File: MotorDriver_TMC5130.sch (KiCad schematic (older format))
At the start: 17 parts, among them U8 TMC5130

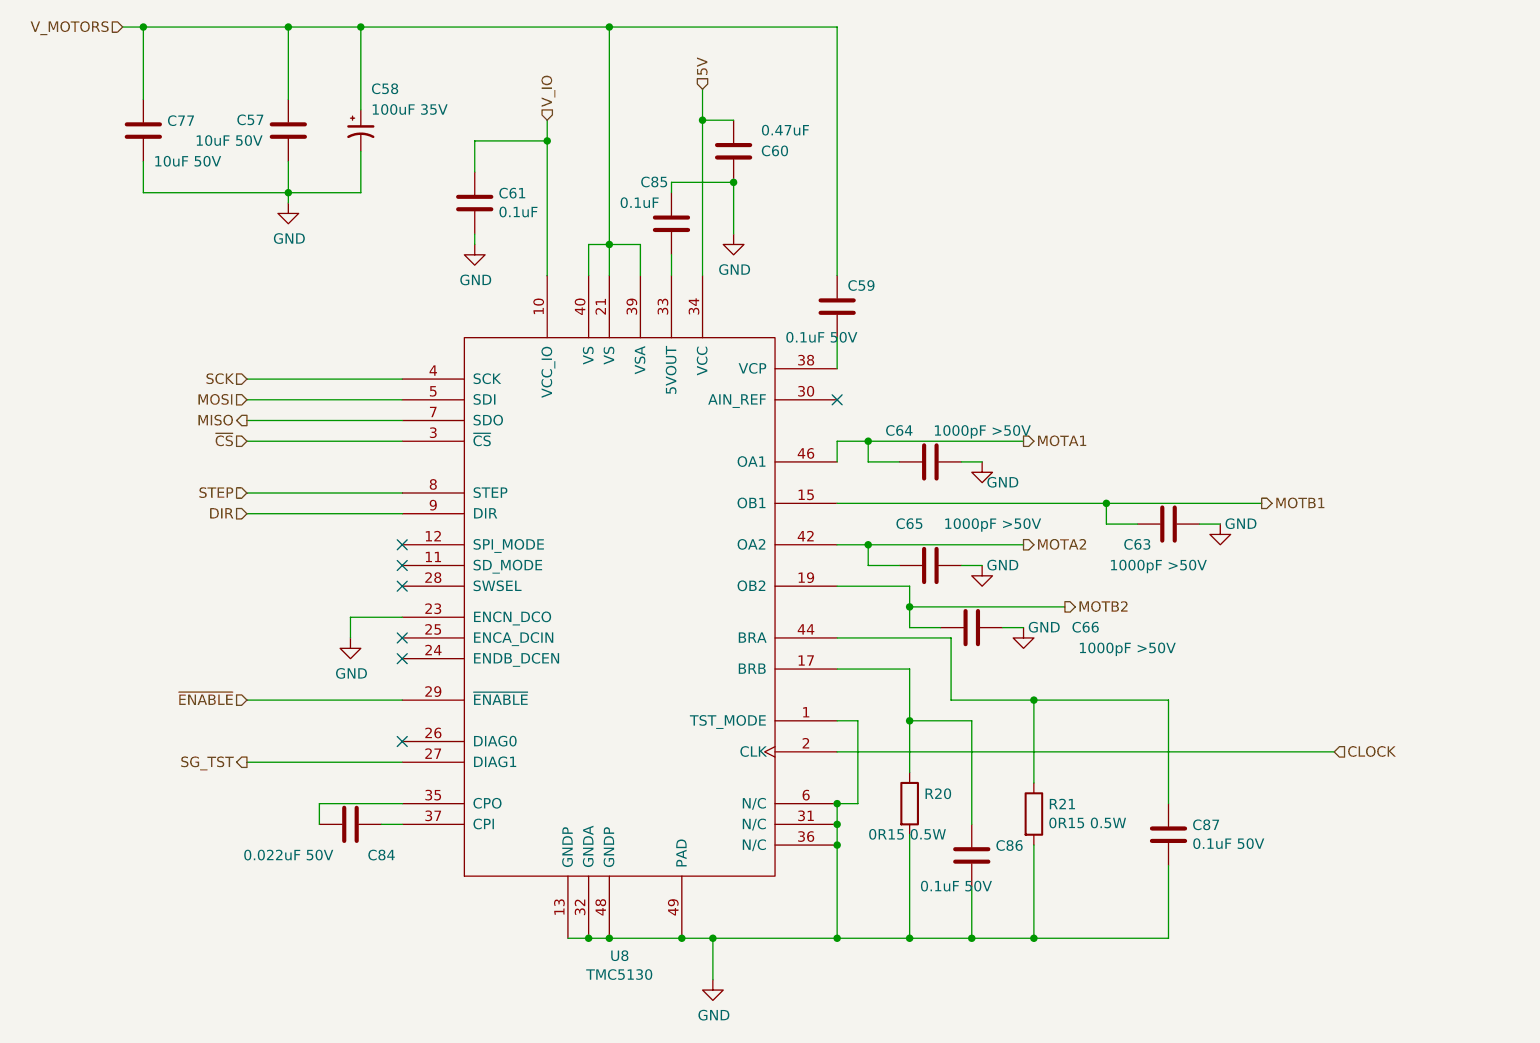
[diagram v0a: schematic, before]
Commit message: Updated schematics with the latest features.
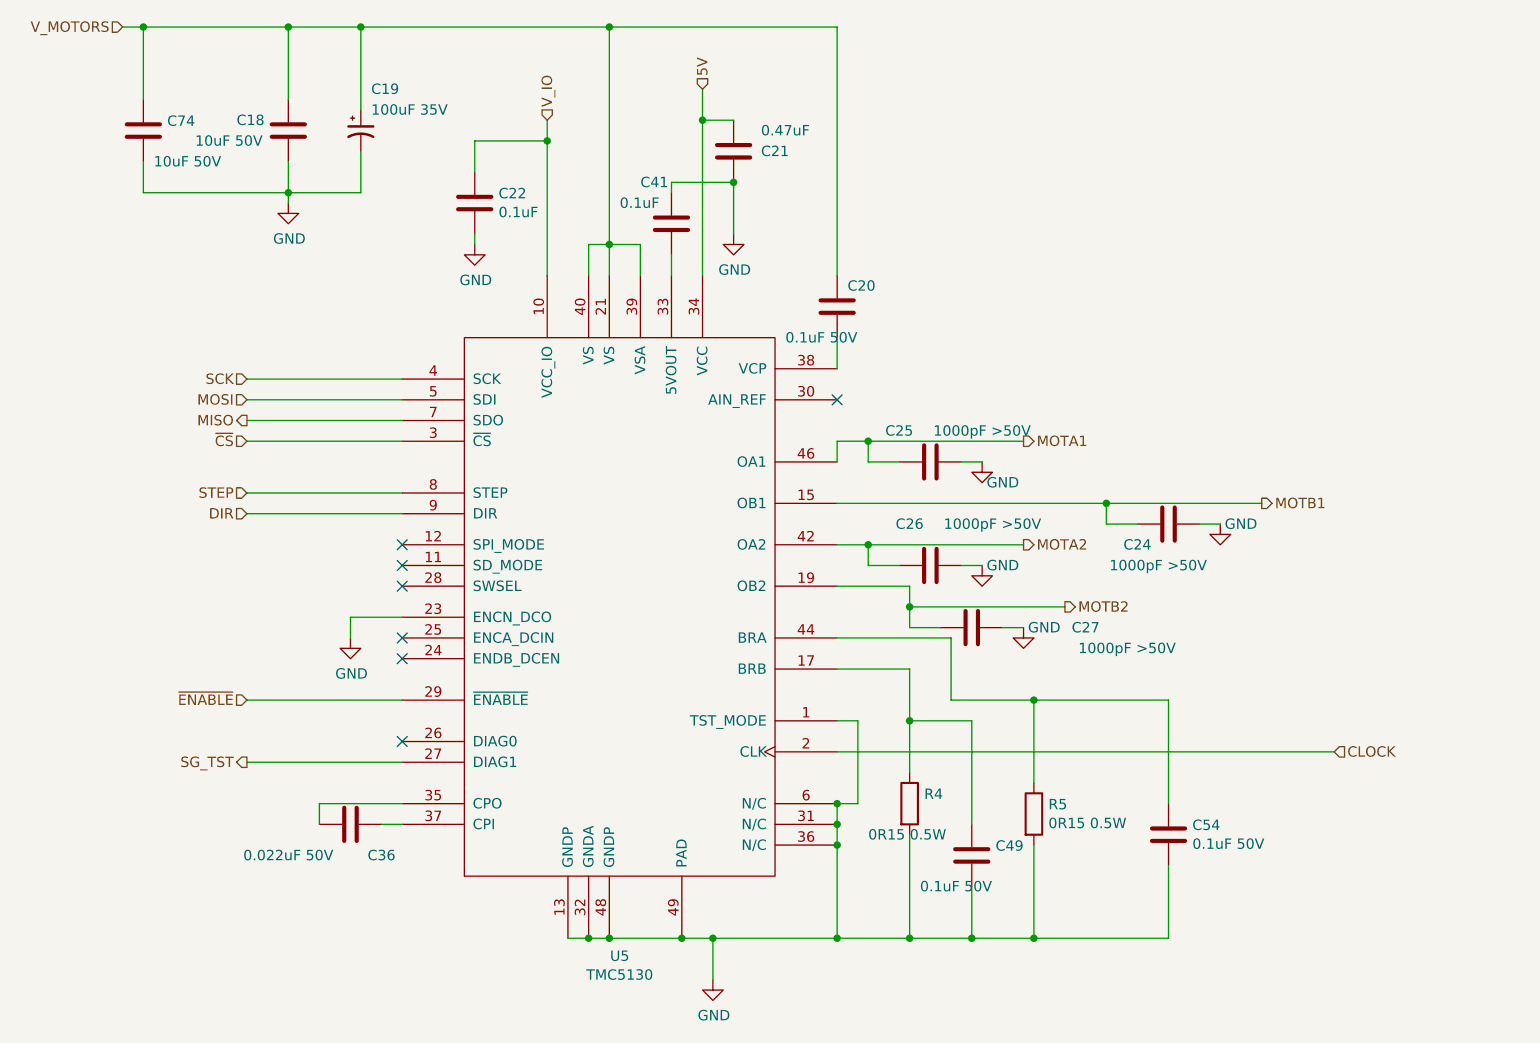
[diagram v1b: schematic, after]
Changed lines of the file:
@@
 $Descr A4 11693 8268
 encoding utf-8
-Sheet 17 35
+Sheet 9 35
 Title ""
 Date ""
@@
 AR Path="/5AC337B6/5ACE1C6D/5ACC0B66/5AC33A94" Ref="C46"  Part="1"
 AR Path="/5AC337B6/5AD9F95A/5AD4B0F5/5AC33A94" Ref="C59"  Part="1"
-F 0 "C59" H 6000 2650 50  0000 L CNN
+F 0 "C20" H 6000 2650 50  0000 L CNN
 F 1 "0.1uF 50V" H 5700 2400 50  0000 L CNN
 F 2 "Capacitor_SMD:C_0402_1005Metric" H 5988 2400 50  0001 C CNN
@@
 AR Path="/5AC337B6/5ACE1C6D/5ACC0B66/5AC33B3C" Ref="C44"  Part="1"
 AR Path="/5AC337B6/5AD9F95A/5AD4B0F5/5AC33B3C" Ref="C57"  Part="1"
-F 0 "C57" H 3050 1750 50  0000 L CNN
+F 0 "C18" H 3050 1750 50  0000 L CNN
 F 1 "10uF 50V" H 2850 1650 50  0000 L CNN
 F 2 "Capacitor_SMD:C_1206_3216Metric" H 3338 1550 50  0001 C CNN
@@
 AR Path="/5AC337B6/5ACE1C6D/5ACC0B66/5AC33B85" Ref="C47"  Part="1"
 AR Path="/5AC337B6/5AD9F95A/5AD4B0F5/5AC33B85" Ref="C60"  Part="1"
-F 0 "C60" H 5250 1800 50  0000 C CNN
+F 0 "C21" H 5250 1800 50  0000 C CNN
 F 1 "0.47uF" H 5200 1700 50  0000 C CNN
 F 2 "Capacitor_SMD:C_0603_1608Metric" H 5488 1650 50  0001 C CNN
@@
 AR Path="/5AC337B6/5ACE1C6D/5ACC0B66/5AC33C56" Ref="C48"  Part="1"
 AR Path="/5AC337B6/5AD9F95A/5AD4B0F5/5AC33C56" Ref="C61"  Part="1"
-F 0 "C61" H 4315 2096 50  0000 L CNN
+F 0 "C22" H 4315 2096 50  0000 L CNN
 F 1 "0.1uF" H 4315 2005 50  0000 L CNN
 F 2 "Capacitor_SMD:C_0603_1608Metric" H 4238 1900 50  0001 C CNN
@@
 AR Path="/5AC337B6/5ACE1C6D/5ACC0B66/5AC33CA1" Ref="C50"  Part="1"
 AR Path="/5AC337B6/5AD9F95A/5AD4B0F5/5AC33CA1" Ref="C63"  Part="1"
-F 0 "C63" V 7650 3450 50  0000 C CNN
+F 0 "C24" V 7650 3450 50  0000 C CNN
 F 1 "1000pF >50V" V 7750 3550 50  0000 C CNN
 F 2 "Capacitor_SMD:C_0603_1608Metric" H 7588 3450 50  0001 C CNN
@@
 AR Path="/5AC337B6/5ACE1C6D/5ACC0B66/5AC33D6E" Ref="C51"  Part="1"
 AR Path="/5AC337B6/5AD9F95A/5AD4B0F5/5AC33D6E" Ref="C64"  Part="1"
-F 0 "C64" V 6250 3150 50  0000 C CNN
+F 0 "C25" V 6250 3150 50  0000 C CNN
 F 1 "1000pF >50V" V 6250 3550 50  0000 C CNN
 F 2 "Capacitor_SMD:C_0603_1608Metric" H 6438 3150 50  0001 C CNN
@@
 AR Path="/5AC337B6/5ACE1C6D/5ACC0B66/5AC33DC1" Ref="C52"  Part="1"
 AR Path="/5AC337B6/5AD9F95A/5AD4B0F5/5AC33DC1" Ref="C65"  Part="1"
-F 0 "C65" V 6200 3700 50  0000 C CNN
+F 0 "C26" V 6200 3700 50  0000 C CNN
 F 1 "1000pF >50V" V 6200 4100 50  0000 C CNN
 F 2 "Capacitor_SMD:C_0603_1608Metric" H 6438 3650 50  0001 C CNN
@@
 AR Path="/5AC337B6/5ACE1C6D/5ACC0B66/5AC33E6E" Ref="C53"  Part="1"
 AR Path="/5AC337B6/5AD9F95A/5AD4B0F5/5AC33E6E" Ref="C66"  Part="1"
-F 0 "C66" V 6600 4650 50  0000 C CNN
+F 0 "C27" V 6600 4650 50  0000 C CNN
 F 1 "1000pF >50V" V 6700 4850 50  0000 C CNN
 F 2 "Capacitor_SMD:C_0603_1608Metric" H 6638 3950 50  0001 C CNN
@@
 AR Path="/5AC337B6/5ACE1C6D/5ACC0B66/5AC34593" Ref="#PWR049"  Part="1"
 AR Path="/5AC337B6/5AD9F95A/5AD4B0F5/5AC34593" Ref="#PWR059"  Part="1"
-F 0 "#PWR059" H 5450 1950 50  0001 C CNN
+F 0 "#PWR027" H 5450 1950 50  0001 C CNN
 F 1 "GND" H 5455 2027 50  0000 C CNN
 F 2 "" H 5450 2200 50  0001 C CNN
@@
 AR Path="/5AC337B6/5ACE1C6D/5ACC0B66/5AC345D6" Ref="#PWR048"  Part="1"
 AR Path="/5AC337B6/5AD9F95A/5AD4B0F5/5AC345D6" Ref="#PWR058"  Part="1"
-F 0 "#PWR058" H 3300 1800 50  0001 C CNN
+F 0 "#PWR026" H 3300 1800 50  0001 C CNN
 F 1 "GND" H 3305 1877 50  0000 C CNN
 F 2 "" H 3300 2050 50  0001 C CNN
@@
 AR Path="/5AC337B6/5ACE1C6D/5ACC0B66/5AC34619" Ref="#PWR050"  Part="1"
 AR Path="/5AC337B6/5AD9F95A/5AD4B0F5/5AC34619" Ref="#PWR060"  Part="1"
-F 0 "#PWR060" H 7800 3350 50  0001 C CNN
+F 0 "#PWR028" H 7800 3350 50  0001 C CNN
 F 1 "GND" H 7900 3600 50  0000 C CNN
 F 2 "" H 7800 3600 50  0001 C CNN
@@
 AR Path="/5AC337B6/5ACE1C6D/5ACC0B66/5AC3465C" Ref="#PWR051"  Part="1"
 AR Path="/5AC337B6/5AD9F95A/5AD4B0F5/5AC3465C" Ref="#PWR061"  Part="1"
-F 0 "#PWR061" H 6650 3050 50  0001 C CNN
+F 0 "#PWR029" H 6650 3050 50  0001 C CNN
 F 1 "GND" H 6750 3200 50  0000 C CNN
 F 2 "" H 6650 3300 50  0001 C CNN
@@
 AR Path="/5AC337B6/5ACE1C6D/5ACC0B66/5AC3469F" Ref="#PWR052"  Part="1"
 AR Path="/5AC337B6/5AD9F95A/5AD4B0F5/5AC3469F" Ref="#PWR062"  Part="1"
-F 0 "#PWR062" H 6650 3550 50  0001 C CNN
+F 0 "#PWR030" H 6650 3550 50  0001 C CNN
 F 1 "GND" H 6750 3800 50  0000 C CNN
 F 2 "" H 6650 3800 50  0001 C CNN
@@
 AR Path="/5AC337B6/5ACE1C6D/5ACC0B66/5AC346E2" Ref="#PWR053"  Part="1"
 AR Path="/5AC337B6/5AD9F95A/5AD4B0F5/5AC346E2" Ref="#PWR063"  Part="1"
-F 0 "#PWR063" H 6850 3850 50  0001 C CNN
+F 0 "#PWR031" H 6850 3850 50  0001 C CNN
 F 1 "GND" H 6950 4100 50  0000 C CNN
 F 2 "" H 6850 4100 50  0001 C CNN
@@
 AR Path="/5AC337B6/5ACE1C6D/5ACC0B66/5AC34725" Ref="#PWR047"  Part="1"
 AR Path="/5AC337B6/5AD9F95A/5AD4B0F5/5AC34725" Ref="#PWR057"  Part="1"
-F 0 "#PWR057" H 5350 5550 50  0001 C CNN
+F 0 "#PWR025" H 5350 5550 50  0001 C CNN
 F 1 "GND" H 5355 5627 50  0000 C CNN
 F 2 "" H 5350 5800 50  0001 C CNN
@@
 AR Path="/5AC337B6/5ACE1C6D/5ACC0B66/5AC55FA7" Ref="C45"  Part="1"
 AR Path="/5AC337B6/5AD9F95A/5AD4B0F5/5AC55FA7" Ref="C58"  Part="1"
-F 0 "C58" H 3700 1900 50  0000 L CNN
+F 0 "C19" H 3700 1900 50  0000 L CNN
 F 1 "100uF 35V" H 3700 1800 50  0000 L CNN
 F 2 "Capacitor_SMD:CP_Elec_6.3x7.7" H 3650 1700 50  0001 C CNN
@@
 AR Path="/5AC337B6/5ACE1C6D/5ACC0B66/5ACA36B2" Ref="C76"  Part="1"
 AR Path="/5AC337B6/5AD9F95A/5AD4B0F5/5ACA36B2" Ref="C77"  Part="1"
-F 0 "C77" H 2715 1746 50  0000 L CNN
+F 0 "C74" H 2715 1746 50  0000 L CNN
 F 1 "10uF 50V" H 2650 1550 50  0000 L CNN
 F 2 "Capacitor_SMD:C_1206_3216Metric" H 2638 1550 50  0001 C CNN
@@
 AR Path="/5AC337B6/5ACCA309/5ACC0B66/5ACFA54E" Ref="U6"  Part="1"
 AR Path="/5AC337B6/5ACE1C6D/5ACC0B66/5ACFA54E" Ref="U7"  Part="1"
-F 0 "U8" H 4900 1714 50  0000 C CNN
+F 0 "U5" H 4900 1714 50  0000 C CNN
 F 1 "TMC5130" H 4900 1623 50  0000 C CNN
 F 2 "PrntrBoardV1:tmc5130-nc" H 4900 3700 50  0001 C CNN
@@
 AR Path="/5AC337B6/5ACCA309/5ACC0B66/5AD3397E" Ref="#PWR081"  Part="1"
 AR Path="/5AC337B6/5ACE1C6D/5ACC0B66/5AD3397E" Ref="#PWR083"  Part="1"
-F 0 "#PWR085" H 4200 2000 50  0001 C CNN
+F 0 "#PWR079" H 4200 2000 50  0001 C CNN
 F 1 "GND" H 4205 2077 50  0000 C CNN
 F 2 "" H 4200 2250 50  0001 C CNN
@@
 AR Path="/5AC337B6/5ACCA309/5ACC0B66/5AD37DE9" Ref="C67"  Part="1"
 AR Path="/5AC337B6/5ACE1C6D/5ACC0B66/5AD37DE9" Ref="C81"  Part="1"
-F 0 "C85" H 5000 2350 50  0000 L CNN
+F 0 "C41" H 5000 2350 50  0000 L CNN
 F 1 "0.1uF" H 4900 2250 50  0000 L CNN
 F 2 "Capacitor_SMD:C_0603_1608Metric" H 5188 2000 50  0001 C CNN
@@
 AR Path="/5AC337B6/5ACCA309/5ACC0B66/5AD494C8" Ref="C62"  Part="1"
 AR Path="/5AC337B6/5ACE1C6D/5ACC0B66/5AD494C8" Ref="C80"  Part="1"
-F 0 "C84" V 3750 5200 50  0000 C CNN
+F 0 "C36" V 3750 5200 50  0000 C CNN
 F 1 "0.022uF 50V" V 3750 4750 50  0000 C CNN
 F 2 "Capacitor_SMD:C_0603_1608Metric" H 3638 4900 50  0001 C CNN
@@
 AR Path="/5AC337B6/5ACCA309/5ACC0B66/5AD5670C" Ref="#PWR080"  Part="1"
 AR Path="/5AC337B6/5ACE1C6D/5ACC0B66/5AD5670C" Ref="#PWR082"  Part="1"
-F 0 "#PWR084" H 3600 3900 50  0001 C CNN
+F 0 "#PWR078" H 3600 3900 50  0001 C CNN
 F 1 "GND" H 3605 3977 50  0000 C CNN
 F 2 "" H 3600 4150 50  0001 C CNN
@@
 AR Path="/5AC337B6/5ACCA309/5ACC0B66/5AD66FAA" Ref="R12"  Part="1"
 AR Path="/5AC337B6/5ACE1C6D/5ACC0B66/5AD66FAA" Ref="R14"  Part="1"
-F 0 "R20" H 6370 4996 50  0000 L CNN
+F 0 "R4" H 6370 4996 50  0000 L CNN
 F 1 "0R15 0.5W" H 6100 4800 50  0000 L CNN
 F 2 "Resistor_SMD:R_1206_3216Metric" V 6230 4950 50  0001 C CNN
@@
 AR Path="/5AC337B6/5ACCA309/5ACC0B66/5AD67008" Ref="R13"  Part="1"
 AR Path="/5AC337B6/5ACE1C6D/5ACC0B66/5AD67008" Ref="R15"  Part="1"
-F 0 "R21" H 6970 5046 50  0000 L CNN
+F 0 "R5" H 6970 5046 50  0000 L CNN
 F 1 "0R15 0.5W" H 6970 4955 50  0000 L CNN
 F 2 "Resistor_SMD:R_1206_3216Metric" V 6830 5000 50  0001 C CNN
@@
 AR Path="/5AC337B6/5ACCA309/5ACC0B66/5AD6F856" Ref="C79"  Part="1"
 AR Path="/5AC337B6/5ACE1C6D/5ACC0B66/5AD6F856" Ref="C83"  Part="1"
-F 0 "C87" H 7665 5146 50  0000 L CNN
+F 0 "C54" H 7665 5146 50  0000 L CNN
 F 1 "0.1uF 50V" H 7665 5055 50  0000 L CNN
 F 2 "Capacitor_SMD:C_0402_1005Metric" H 7588 4950 50  0001 C CNN
@@
 AR Path="/5AC337B6/5ACCA309/5ACC0B66/5AD6F966" Ref="C78"  Part="1"
 AR Path="/5AC337B6/5ACE1C6D/5ACC0B66/5AD6F966" Ref="C82"  Part="1"
-F 0 "C86" H 6715 5246 50  0000 L CNN
+F 0 "C49" H 6715 5246 50  0000 L CNN
 F 1 "0.1uF 50V" H 6350 5050 50  0000 L CNN
 F 2 "Capacitor_SMD:C_0402_1005Metric" H 6638 5050 50  0001 C CNN

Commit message: Add missing files from the TMC2130 branch.
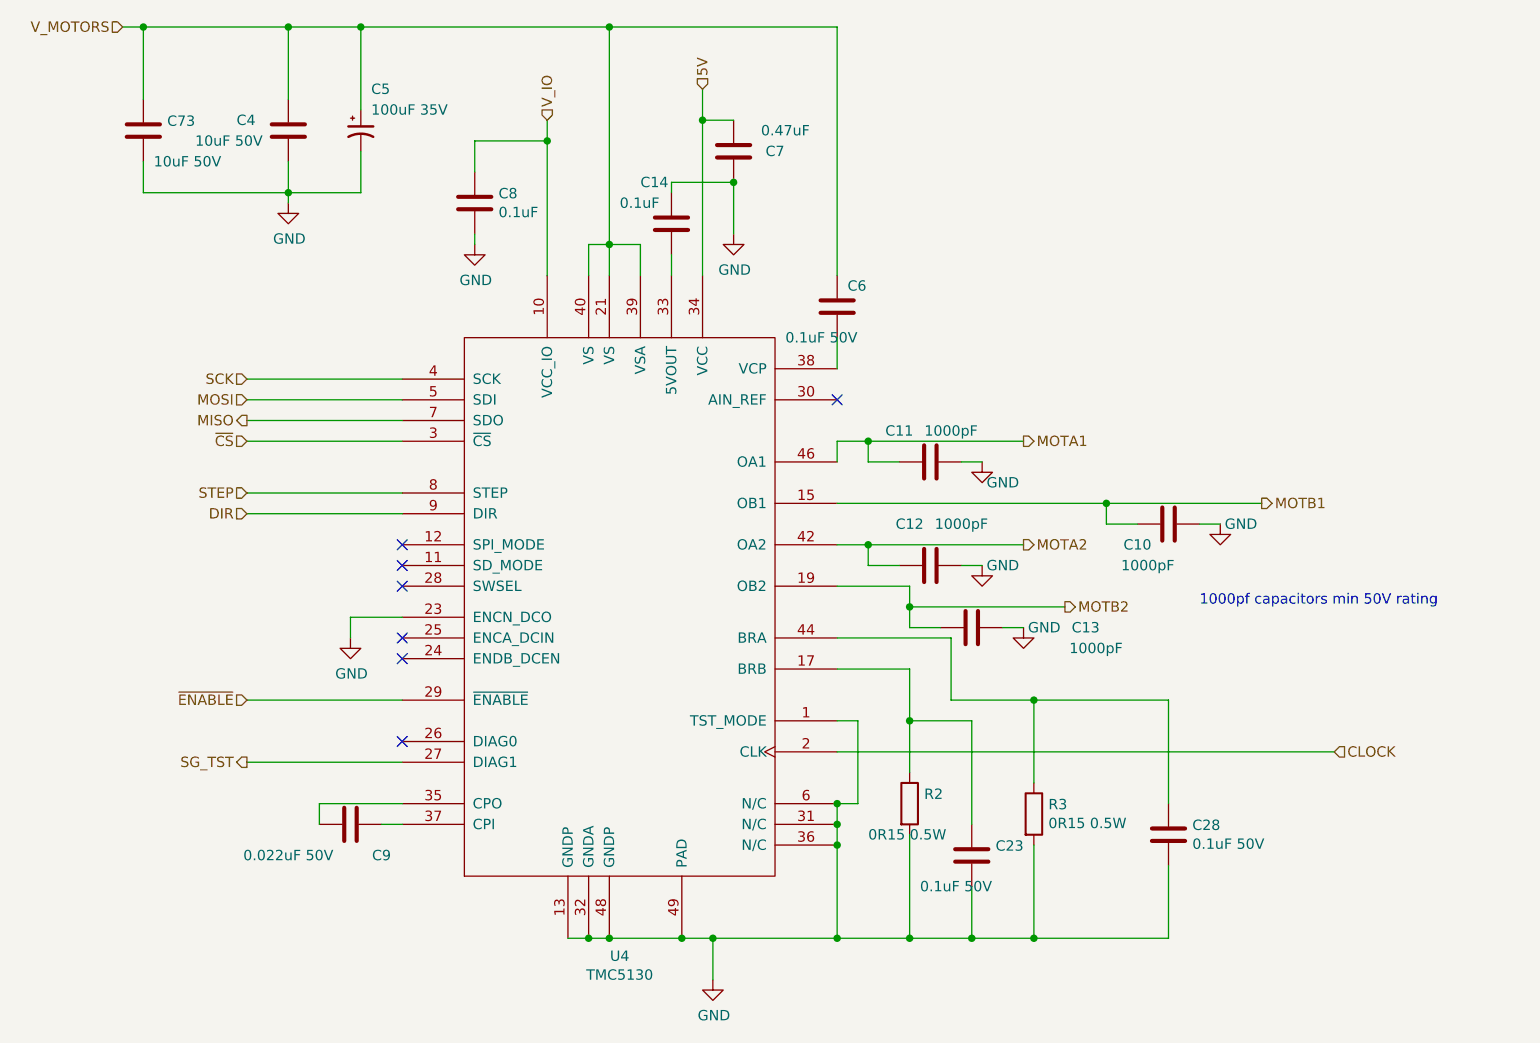
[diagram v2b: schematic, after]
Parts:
- C10, C11, C12, C13: value 1000pF >50V -> 1000pF; footprint Capacitor_SMD:C_0603_1608Metric -> PrntrBoardV1:C_0603_1608Metric
- C4, C74: footprint Capacitor_SMD:C_1206_3216Metric -> PrntrBoardV1:C_1206_3216Metric
- C6, C86, C87: footprint Capacitor_SMD:C_0402_1005Metric -> PrntrBoardV1:C_0402_1005Metric
- C7, C8, C84, C85: footprint Capacitor_SMD:C_0603_1608Metric -> PrntrBoardV1:C_0603_1608Metric
- R20, R21: footprint Resistor_SMD:R_1206_3216Metric -> PrntrBoardV1:R_1206_3216Metric
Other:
- note added: "1000pf capacitors min 50V rating"
